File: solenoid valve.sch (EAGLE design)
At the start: 114 parts, among them CN1 8P8C-LED, IC1 IRFR320PBF, IC2 IRFR320PBF, IC3 IRFR320PBF, IC4 IRFR320PBF, IC5 IRFR320PBF, IC6 IRFR320PBF, IC7 IRFR320PBF, J1 XT30UPB-M, Q10 TLP291_SE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

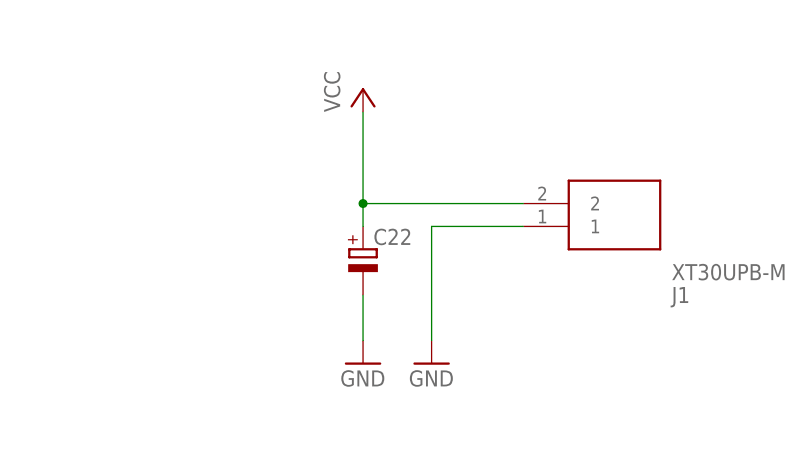
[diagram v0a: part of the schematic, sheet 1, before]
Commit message: ERC and DRC check
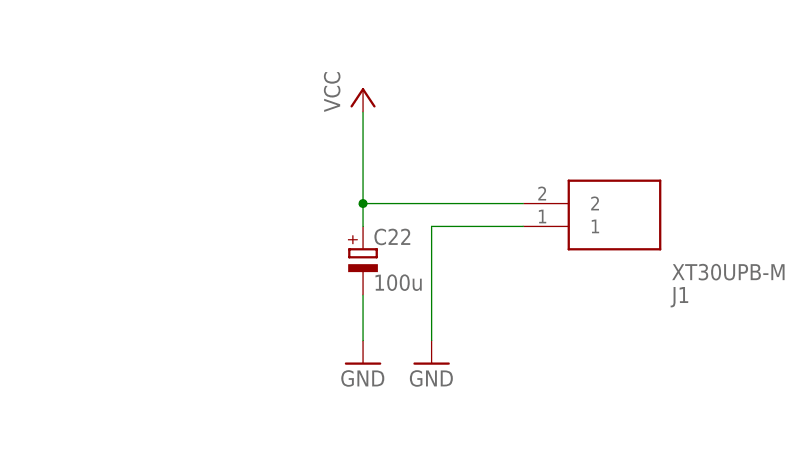
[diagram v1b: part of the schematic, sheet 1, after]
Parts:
- C22: value (none) -> 100u
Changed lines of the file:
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@@
 <part name="GND27" library="supply1" library_urn="urn:adsk.eagle:library:371" deviceset="GNDIO" device=""/>
 <part name="GND36" library="supply1" library_urn="urn:adsk.eagle:library:371" deviceset="GNDIO" device=""/>
-<part name="C22" library="rcl" library_urn="urn:adsk.eagle:library:334" deviceset="CPOL-EU" device="E2-5" package3d_urn="urn:adsk.eagle:package:23346/2"/>
+<part name="C22" library="rcl" library_urn="urn:adsk.eagle:library:334" deviceset="CPOL-EU" device="E2-5" package3d_urn="urn:adsk.eagle:package:23346/2" value="100u"/>
 <part name="GND50" library="supply1" library_urn="urn:adsk.eagle:library:371" deviceset="GND" device=""/>
 <part name="GND54" library="supply1" library_urn="urn:adsk.eagle:library:371" deviceset="GND" device=""/>
@@
 </sheet>
 </sheets>
+<errors>
+</errors>
 </schematic>
 </drawing>
